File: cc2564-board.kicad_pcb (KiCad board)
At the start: 4 copper layers, 25.9 x 67.9 mm, 69 parts, among them J1 TYPE-C-31-M-12, J2 Conn_ARM_JTAG_SWD_10, J3 Conn_01x16, J4 Conn_01x16, J5 BOOT, J6 1909763-1, J7 Conn_01x04, SW1 SW_Push, U1 TLV7111833DDSET, U2 USBLC6-2P6, U3 STM32F103C8Tx, U4 TXB0108DQSR, U5 CC2564CRVMR, Y1 ECS-80-18-30-JGN-TR, Y2 ECS-327MVATX-3-CN-TR, Y3 ECS-260-8-36CKM-TR

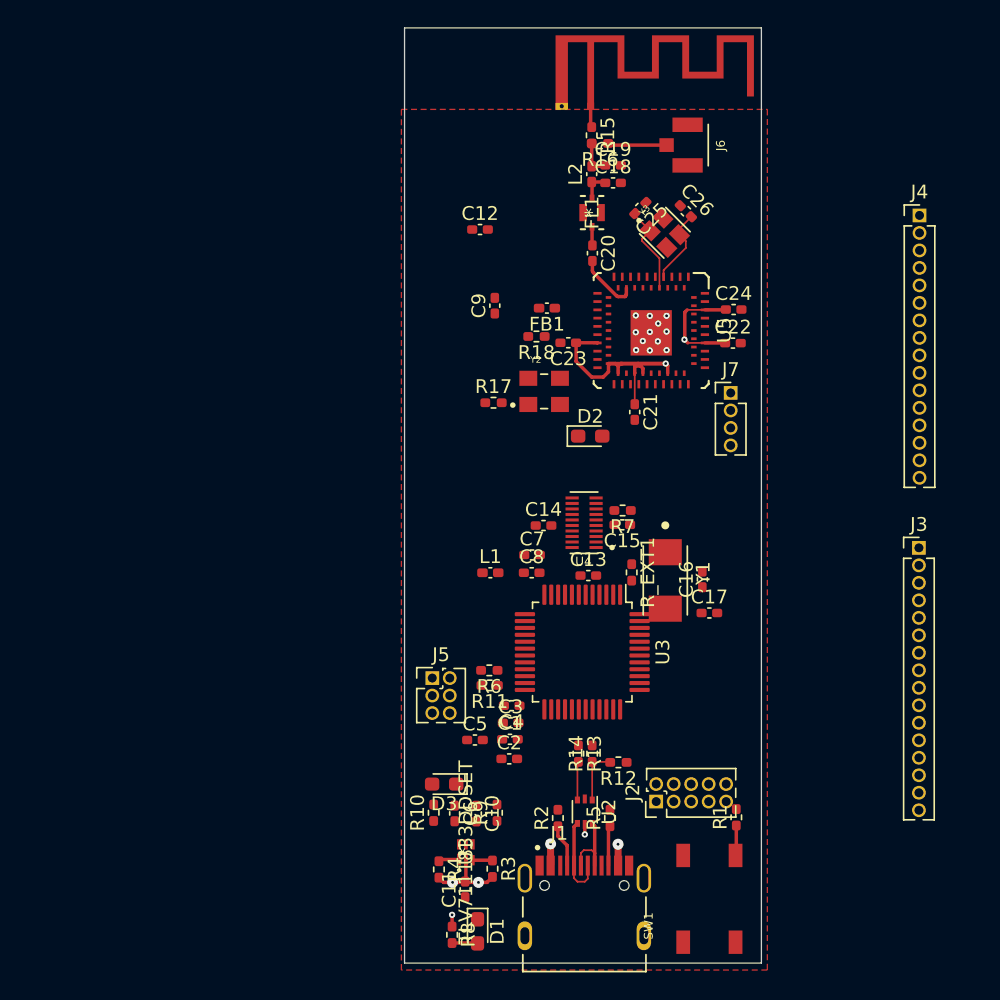
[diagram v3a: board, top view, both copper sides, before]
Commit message: Finish most BT stuff
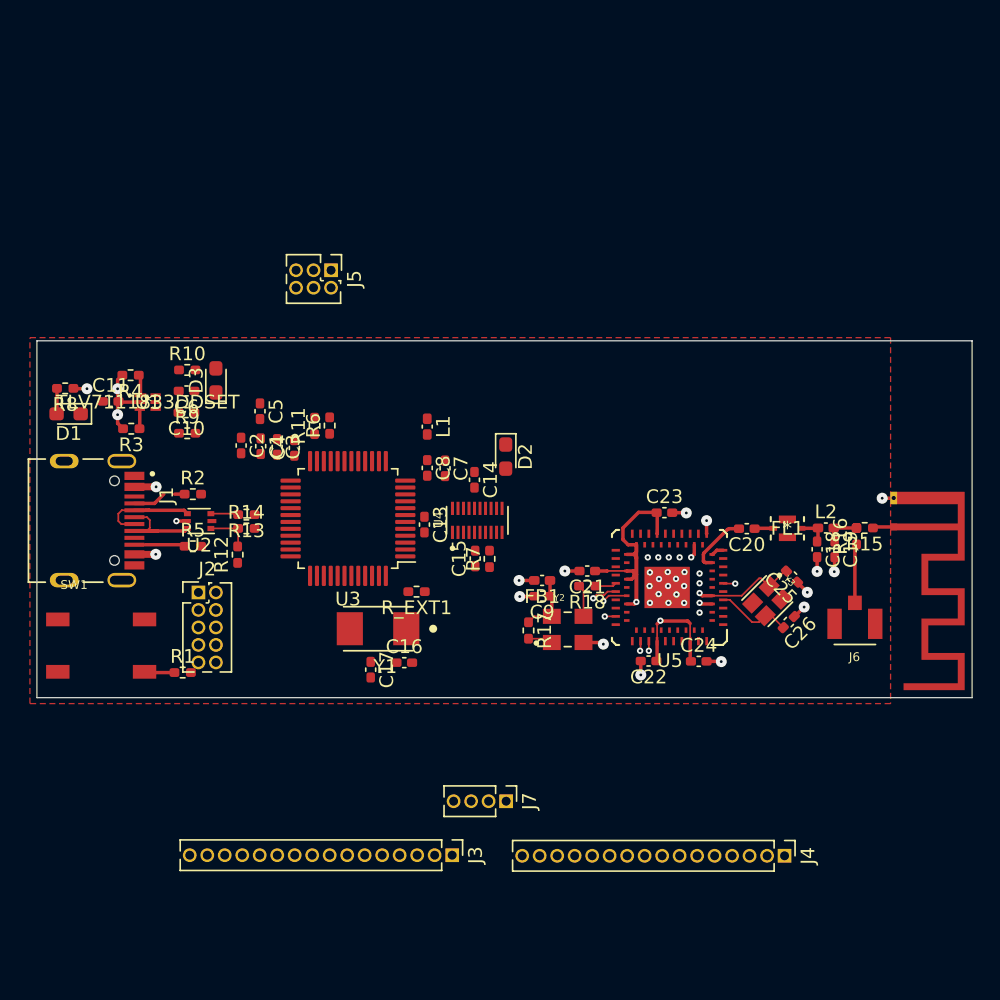
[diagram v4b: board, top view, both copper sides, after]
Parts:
- removed C12: 0.1uF, Capacitor_SMD:C_0402_1005Metric_Pad0.74x0.62mm_HandSolder
- moved R8 48.6 mm to (134.5, 78.5), turned to 180 degrees
- moved J1 48.3 mm to (134.5, 88.1), turned to -90 degrees
- moved D1 47.9 mm to (134.8, 80.3), turned to 180 degrees
- moved SW1 47.8 mm to (137.1, 97.2), turned to 0 degrees
- moved J4 47.5 mm to (186.8, 112.4), turned to -90 degrees
- moved C11 43.8 mm to (137.8, 79.4), turned to 0 degrees
- moved R4 42.3 mm to (139.3, 77.5), turned to 180 degrees
- moved R1 41.5 mm to (143.1, 99.1), turned to 0 degrees
- moved R3 41.3 mm to (139.3, 81.4), turned to 180 degrees
- moved J3 40.6 mm to (162.6, 112.4), turned to -90 degrees
- moved U1 40.0 mm to (140.5, 79.5), turned to 0 degrees
- moved AE1 37.6 mm to (194.7, 88.5), turned to -90 degrees
- moved J6 36.8 mm to (191.9, 95.6), turned to 180 degrees
- moved R10 36.8 mm to (143.4, 77.1), turned to 0 degrees
- moved J2 36.5 mm to (144.2, 93.3), turned to 0 degrees
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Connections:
- C25 pad 2: Net-(C25-Pad2) -> GND
- J1 pad A8: no_connect_78 -> no_connect_76
- J1 pad B8: no_connect_79 -> no_connect_77
- J2 pad 8: no_connect_80 -> no_connect_78
- U3 pad 2: no_connect_81 -> no_connect_79
- U3 pad 3: no_connect_82 -> no_connect_80
- U3 pad 4: no_connect_83 -> no_connect_81
- U4 pad 10: no_connect_84 -> no_connect_82
- U4 pad 11: no_connect_85 -> no_connect_83
- U4 pad 12: no_connect_86 -> no_connect_84
- U4 pad 13: no_connect_87 -> no_connect_85
- U4 pad 8: no_connect_88 -> no_connect_86
- U4 pad 9: no_connect_89 -> no_connect_87
- U5 pad A1: no_connect_90 -> no_connect_88
- U5 pad A12: no_connect_91 -> no_connect_89
- U5 pad A13: no_connect_92 -> no_connect_90
- U5 pad A14: no_connect_93 -> no_connect_91
- U5 pad A15: no_connect_94 -> no_connect_92
- U5 pad A16: no_connect_95 -> no_connect_93
- U5 pad A18: no_connect_96 -> no_connect_94
- U5 pad A19: no_connect_97 -> no_connect_95
- U5 pad A2: no_connect_98 -> no_connect_96
- U5 pad A20: no_connect_99 -> no_connect_97
- U5 pad A21: no_connect_100 -> no_connect_98
- U5 pad A22: no_connect_101 -> no_connect_99
- U5 pad A23: no_connect_102 -> no_connect_100
- U5 pad A27: no_connect_103 -> no_connect_101
- U5 pad A3: no_connect_104 -> no_connect_102
- U5 pad A30: no_connect_105 -> no_connect_103
- U5 pad A31: no_connect_106 -> no_connect_104
- U5 pad A35: no_connect_107 -> no_connect_105
- U5 pad A36: no_connect_108 -> no_connect_106
- U5 pad A37: no_connect_109 -> no_connect_107
- U5 pad A39: no_connect_110 -> no_connect_108
- U5 pad A40: no_connect_111 -> no_connect_109
- U5 pad A5: no_connect_112 -> no_connect_110
- U5 pad A7: no_connect_113 -> no_connect_111
- U5 pad A8: no_connect_114 -> no_connect_112
- U5 pad A9: no_connect_115 -> no_connect_113
- U5 pad B1: no_connect_116 -> no_connect_114
- U5 pad B10: no_connect_117 -> no_connect_115
- U5 pad B12: no_connect_118 -> no_connect_116
- U5 pad B13: no_connect_119 -> no_connect_117
- U5 pad B14: no_connect_120 -> no_connect_118
- U5 pad B15: no_connect_121 -> no_connect_119
- U5 pad B16: no_connect_122 -> no_connect_120
- U5 pad B17: no_connect_123 -> no_connect_121
- U5 pad B2: no_connect_124 -> no_connect_122
- U5 pad B20: no_connect_125 -> no_connect_123
- U5 pad B23: no_connect_126 -> no_connect_124
- U5 pad B26: no_connect_127 -> no_connect_125
- U5 pad B27: no_connect_128 -> no_connect_126
- U5 pad B28: no_connect_129 -> no_connect_127
- U5 pad B29: no_connect_130 -> no_connect_128
- U5 pad B30: no_connect_131 -> no_connect_129
- U5 pad B31: no_connect_132 -> no_connect_130
- U5 pad B32: no_connect_133 -> no_connect_131
- U5 pad B33: no_connect_134 -> no_connect_132
- U5 pad B34: no_connect_135 -> no_connect_133
- U5 pad B35: no_connect_136 -> no_connect_134
- U5 pad B36: no_connect_137 -> no_connect_135
- U5 pad B4: Net-(C25-Pad2) -> GND
- U5 pad B5: no_connect_138 -> no_connect_136
- U5 pad B6: no_connect_139 -> no_connect_137
- U5 pad B7: no_connect_140 -> no_connect_138
- Y3 pad 1: Net-(C25-Pad2) -> GND
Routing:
- net GND: track 0.00 -> 23.2 mm, vias 7 -> 35
- net Net-(C25-Pad2): track 6.62 -> 0.00 mm
- net VDD_1V8_32K: track 0.00 -> 4.54 mm
- net USB_CONN_D+: track 5.23 -> 8.59 mm
- net Net-(R18-Pad2): track 0.00 -> 2.33 mm
- net BT_TX_DBG: track 0.00 -> 1.86 mm, vias 0 -> 1
- net BT_SLOW_CLK: track 0.00 -> 1.84 mm
- net USART2_TX_1V8: track 0.00 -> 1.84 mm, vias 0 -> 1
- net Net-(R17-Pad2): track 0.00 -> 1.81 mm
- net VDD_1V8: track 28.8 -> 30.0 mm, vias 2 -> 3
- net USB_CONN_D-: track 6.23 -> 7.30 mm
- net NSHUTDOWN_1V8: track 0.00 -> 0.88 mm, vias 0 -> 1
- net USART2_RTS_1V8: track 0.00 -> 0.80 mm, vias 0 -> 1
- net USB_D+: track 4.09 -> 3.31 mm
- net USB_D-: track 2.80 -> 2.01 mm
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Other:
- board size 25.9 x 67.9 mm -> 67.9 x 25.9 mm
